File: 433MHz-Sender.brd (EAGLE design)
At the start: 33 x 47 mm, 21 parts, among them IC1 LP2950Z, U1 ATTINY85V-10S

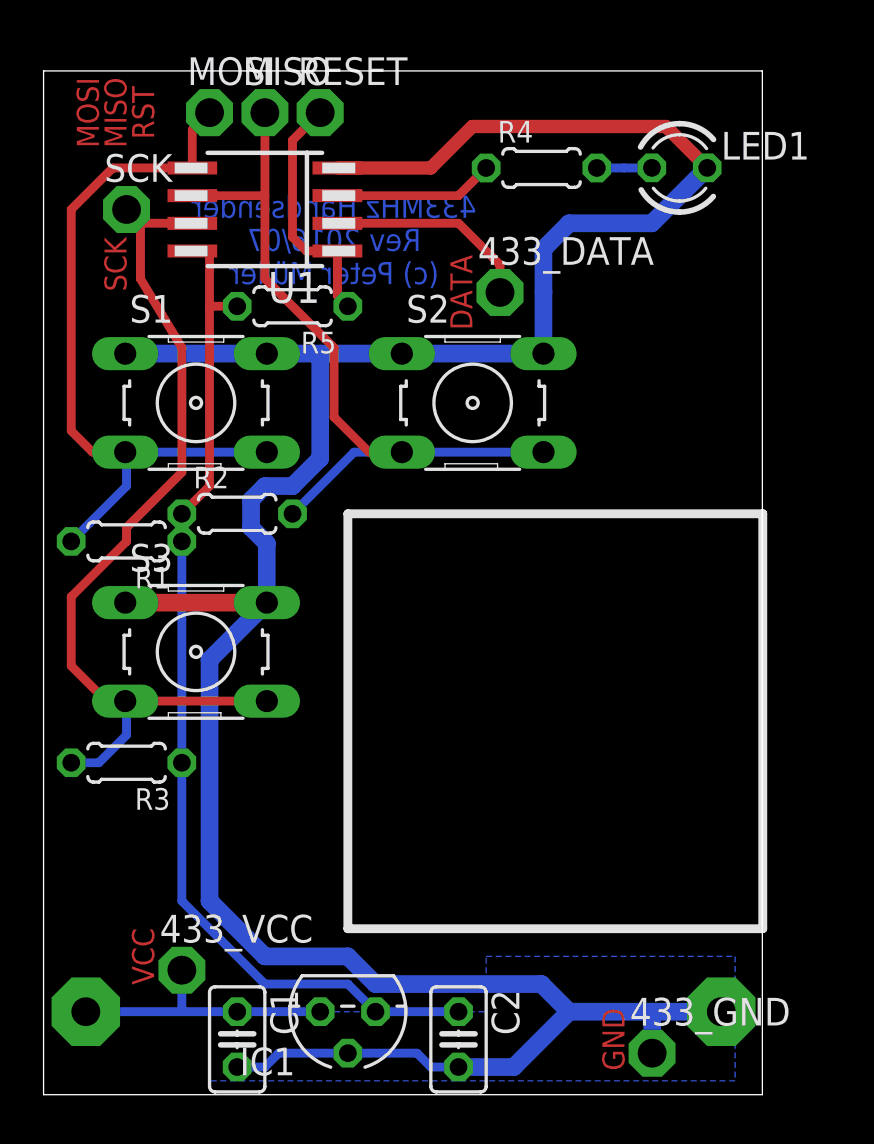
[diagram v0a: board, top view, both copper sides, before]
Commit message: 433MHz-Server und IO-Board-2 Anpassungen
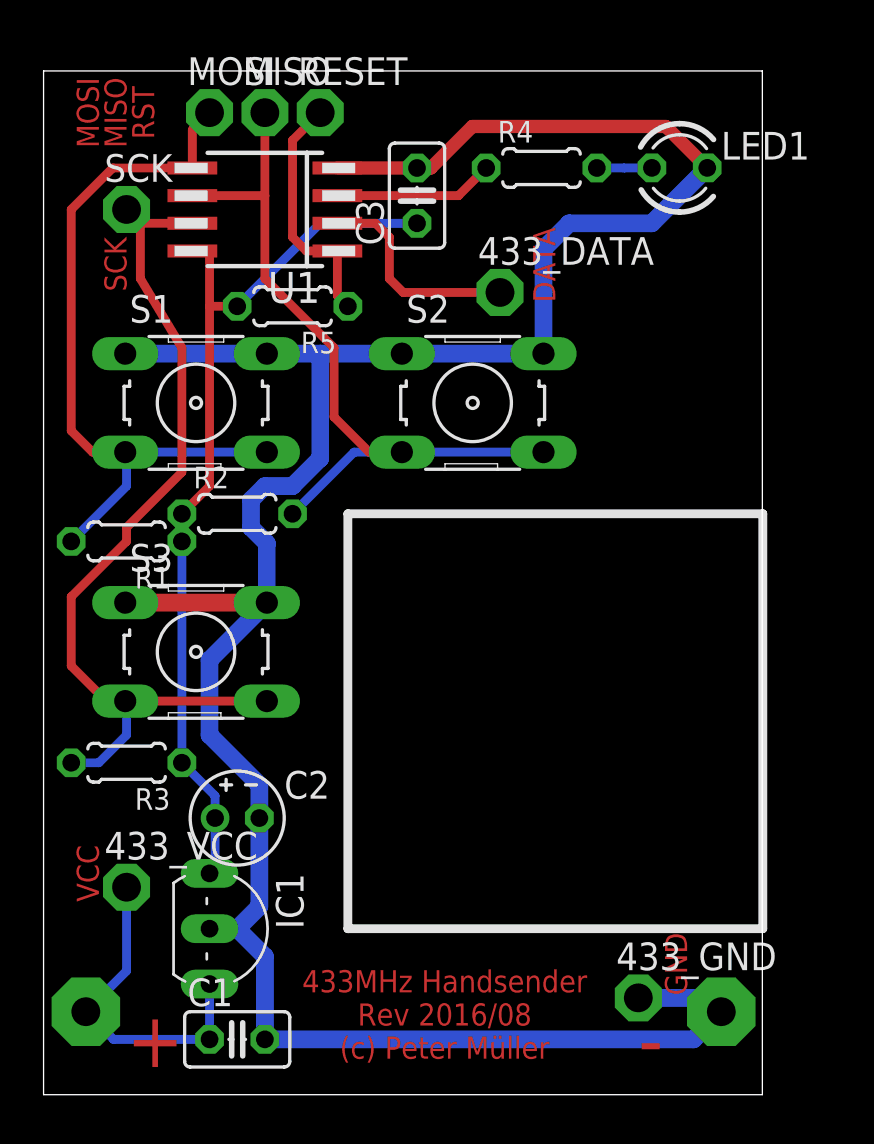
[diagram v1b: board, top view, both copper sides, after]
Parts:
- added C3: 100nF, rcl:C025-025X050
- C1: value 1µF -> 100nF
- C2: value 2,2µF -> 10µF; device rcl:C025-025X050 -> rcl:E2-4
- IC1: value LP2950Z -> LM2936-5.0; device linear:TO92 -> LM2936:TO92-INLINE
- moved C2 14.4 mm to (8.89, 12.7), turned to 0 degrees
- moved IC1 7.41 mm to (7.62, 7.62), turned to 270 degrees
- moved 433_VCC 4.58 mm to (3.81, 9.53)
- moved 433_GND 2.62 mm to (27.3, 4.45)
- turned C1 to 0 degrees
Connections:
- net +12V: now also IC1.VIN; no longer IC1.3
- net +5V: now also C2.+, C3.1, IC1.VO; no longer C2.1, IC1.1
- net GND: now also C2.-, C3.2, IC1.GND; no longer C2.2, IC1.2
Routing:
- net GND: track 131.2 -> 122.3 mm
- net +5V: track 47.2 -> 41.7 mm
- net +12V: track 12.7 -> 15.2 mm
- removed copper zone on layer 16, net GND
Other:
- board text added: "+"
- board text added: "-"
- board text added: "433MHz Handsender Rev 2016/08 (c) Peter Müller"
- board text removed: "433MHz Handsender Rev 2016/07 (c) Peter Müller"

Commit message: IO-Board-2 Anpassung
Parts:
- R1, R2, R3: value 10k -> 100k
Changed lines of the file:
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@@
 <element name="G1" library="bat-gp23a" package="GP23A" value="GP23A" x="15.24" y="-3.81" rot="MR0"/>
 <element name="LED1" library="led" package="LED3MM" value="" x="29.2" y="42.55"/>
-<element name="R1" library="rcl" package="0204/5" value="10k" x="3.81" y="25.4" rot="R180"/>
-<element name="R2" library="rcl" package="0204/5" value="10k" x="8.89" y="26.67"/>
-<element name="R3" library="rcl" package="0204/5" value="10k" x="3.81" y="15.24" rot="R180"/>
+<element name="R1" library="rcl" package="0204/5" value="100k" x="3.81" y="25.4" rot="R180"/>
+<element name="R2" library="rcl" package="0204/5" value="100k" x="8.89" y="26.67"/>
+<element name="R3" library="rcl" package="0204/5" value="100k" x="3.81" y="15.24" rot="R180"/>
 <element name="R4" library="rcl" package="0204/5" value="1k5" x="22.86" y="42.545"/>
 <element name="S1" library="switch-omron" package="B3F-10XX" value="" x="7" y="31.76">
